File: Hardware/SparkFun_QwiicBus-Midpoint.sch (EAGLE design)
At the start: 39 parts, among them J1 QWIIC, J2 QWIIC, J3 RJ45, J7 RJ45, U1 PCA9615, U2 3.3V

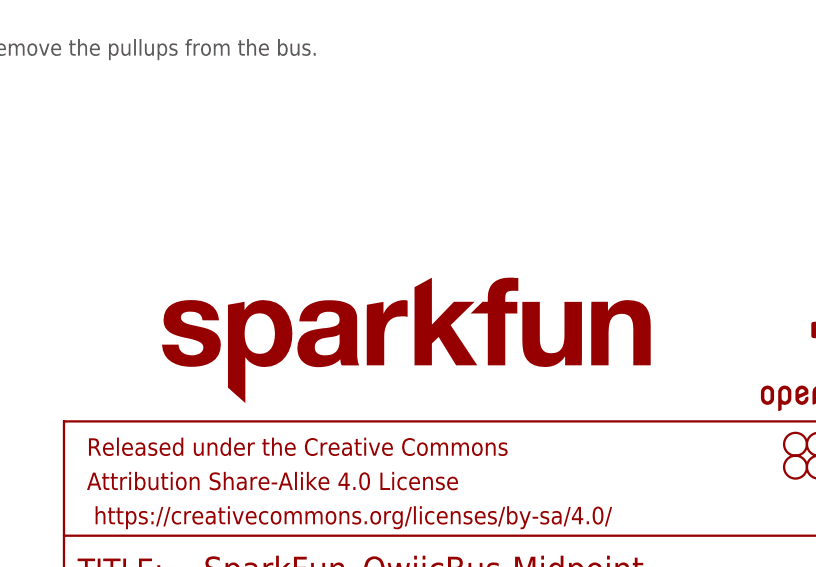
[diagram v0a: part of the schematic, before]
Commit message: adding qwiicBus silk
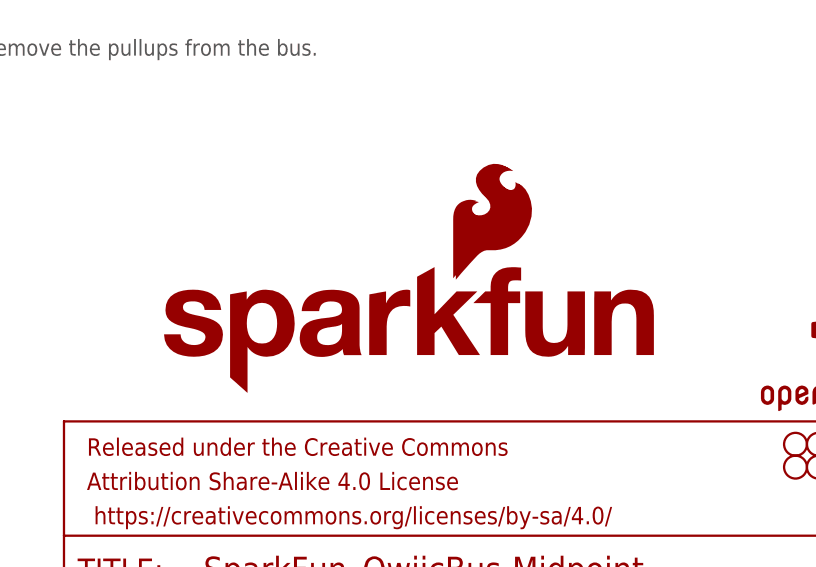
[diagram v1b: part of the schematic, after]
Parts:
- removed LOGO5: SFE_LOGO_NAME.1_INCH, SparkFun-Aesthetics:SFE_LOGO_NAME.1_INCH
- added LOGO3: SFE_LOGO_FLAME.2_INCH, SparkFun-Aesthetics:SFE_LOGO_FLAME.2_INCH
- added LOGO4: SFE_LOGO_NAME_FLAME.1_INCH, SparkFun-Aesthetics:SFE_LOGO_NAME_FLAME.1_INCH
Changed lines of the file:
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@@
 <part name="FD3" library="SparkFun-Aesthetics" deviceset="FIDUCIAL" device="UFIDUCIAL"/>
 <part name="FD4" library="SparkFun-Aesthetics" deviceset="FIDUCIAL" device="UFIDUCIAL"/>
-<part name="LOGO5" library="SparkFun-Aesthetics" deviceset="SFE_LOGO_NAME" device=".1_INCH"/>
 <part name="J7" library="SparkFun-Connectors" deviceset="RJ45-8" device="" value="RJ45"/>
 <part name="GND13" library="SparkFun-PowerSymbols" deviceset="GND" device=""/>
@@
 <part name="J5" library="SparkFun-Connectors" deviceset="CONN_04" device="1X04_NO_SILK"/>
 <part name="J6" library="SparkFun-Connectors" deviceset="CONN_02" device="1X02_NO_SILK"/>
+<part name="LOGO3" library="SparkFun-Aesthetics" deviceset="SFE_LOGO_FLAME" device=".2_INCH" value="SFE_LOGO_FLAME.2_INCH"/>
+<part name="LOGO4" library="SparkFun-Aesthetics" deviceset="SFE_LOGO_NAME_FLAME" device=".1_INCH"/>
 </parts>
 <sheets>
@@
 <instance part="FD3" gate="G$1" x="243.84" y="33.02" smashed="yes"/>
 <instance part="FD4" gate="G$1" x="243.84" y="30.48" smashed="yes"/>
-<instance part="LOGO5" gate="G$1" x="156.21" y="37.592" smashed="yes"/>
 <instance part="J7" gate="JP1" x="210.82" y="144.78" smashed="yes">
 <attribute name="NAME" x="205.74" y="155.448" size="1.778" layer="95" font="vector"/>
@@
 <attribute name="NAME" x="53.34" y="13.208" size="1.778" layer="95" font="vector"/>
 </instance>
+<instance part="LOGO3" gate="G$1" x="190.5" y="50.8" smashed="yes"/>
+<instance part="LOGO4" gate="G$1" x="157.734" y="38.354" smashed="yes"/>
 </instances>
 <busses>

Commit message: pushing mid checklist changes
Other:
- note added: "v11"
- note removed: "v10"
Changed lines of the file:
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@@
 <wire x1="88.9" y1="114.3" x2="0" y2="114.3" width="0.2032" layer="97" style="longdash"/>
 <wire x1="88.9" y1="185.42" x2="88.9" y2="114.3" width="0.2032" layer="97" style="longdash"/>
-<text x="238.76" y="7.62" size="2.54" layer="94" font="vector">v10</text>
+<text x="238.76" y="7.62" size="2.54" layer="94" font="vector">v11</text>
 <wire x1="88.9" y1="81.28" x2="0" y2="81.28" width="0.2032" layer="97" style="longdash"/>
 <text x="114.3" y="76.2" size="1.778" layer="97" font="vector">Cut the I2C jumper to remove the pullups from the bus.</text>

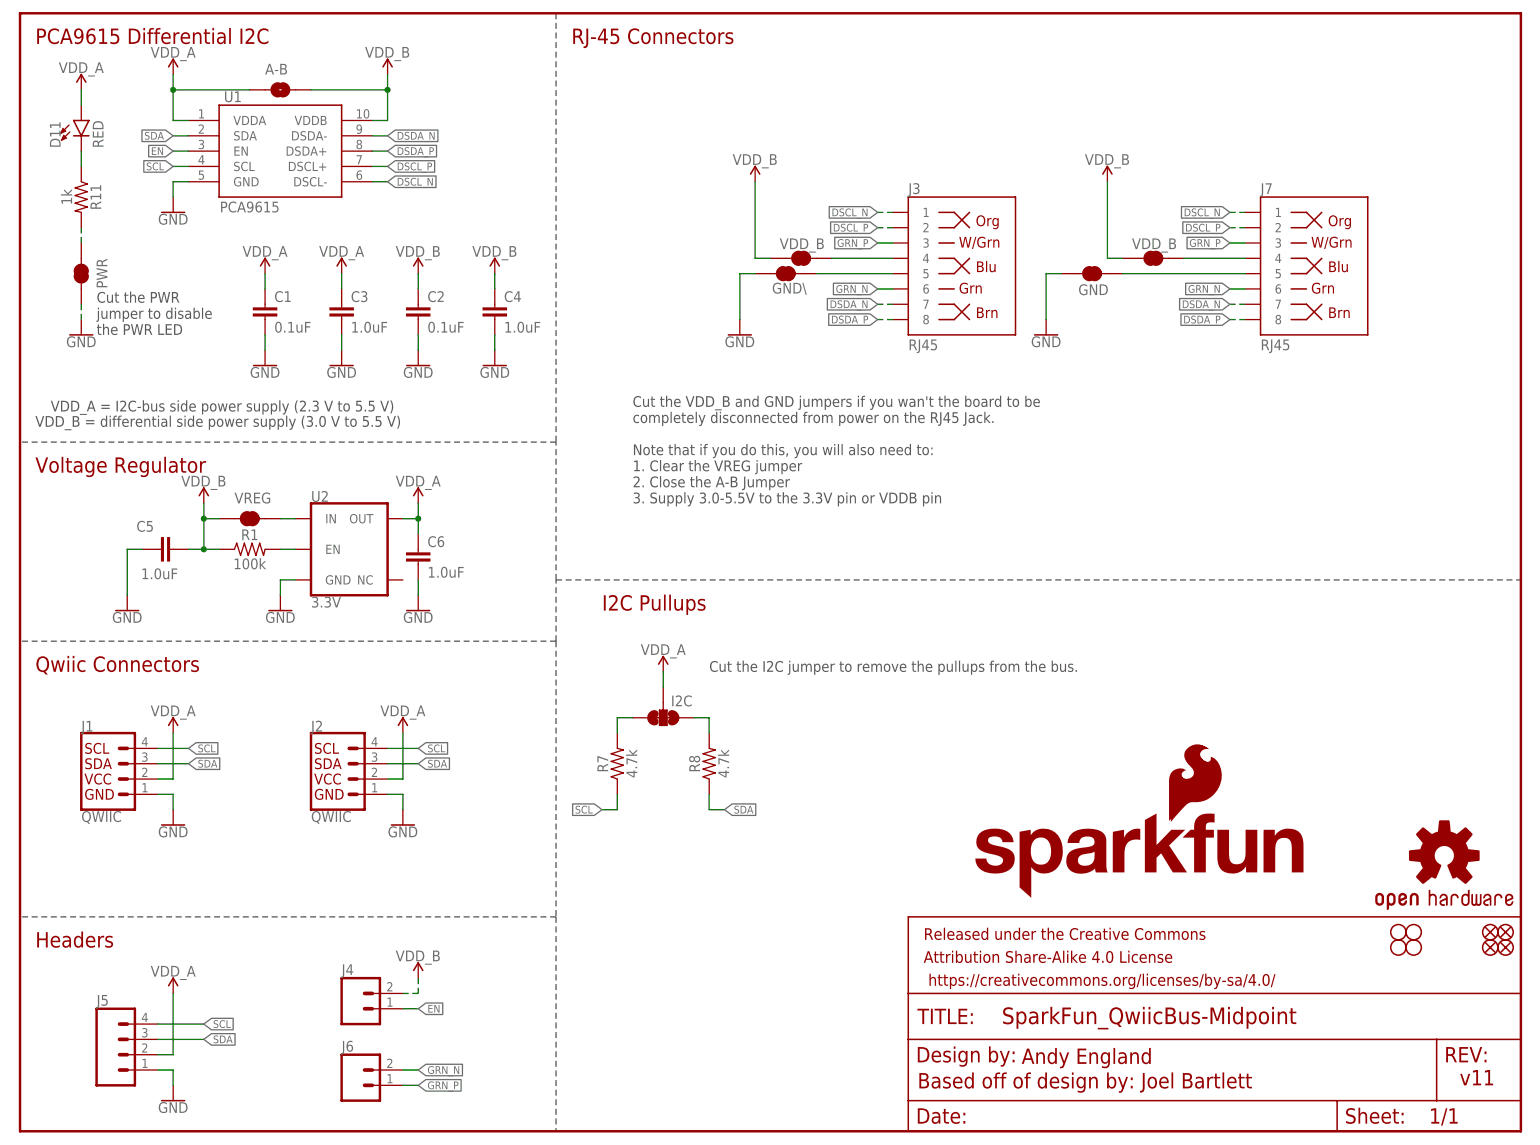
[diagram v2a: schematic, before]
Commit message: adding buck regulator
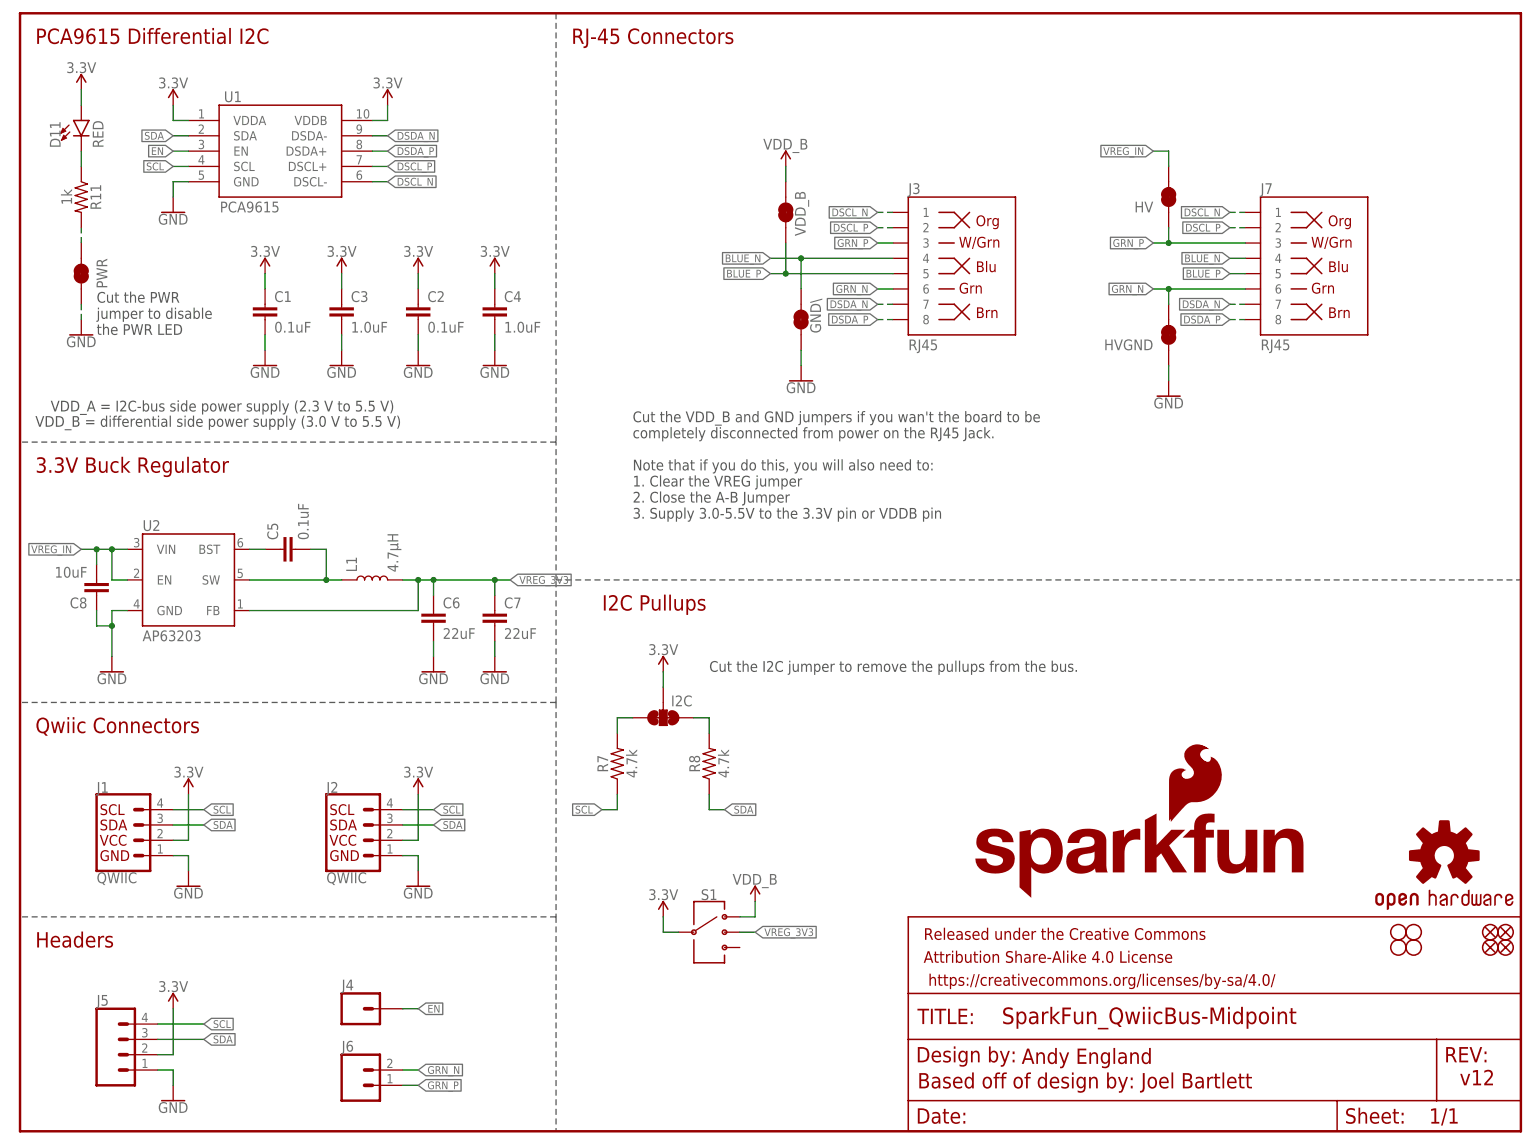
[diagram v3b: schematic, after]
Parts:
- removed A-B: JUMPER-SMT_2_NO_SILK, SparkFun-Jumpers:JUMPER-SMT_2_NO_SILK
- removed JP5, JP6, VREG: JUMPER-SMT_2_NC_TRACE_SILK, SparkFun-Jumpers:JUMPER-SMT_2_NC_TRACE_SILK
- removed R1: 100k, SparkFun-Resistors:100KOHM-0603-1/10W-1%
- added C7: 22uF, SparkFun-Capacitors:22UF-1206-50V-10%
- added C8: 10uF, SparkFun-Capacitors:10UF-1210-50V-20%
- added HV, HVGND: JUMPER-SMT_2_NC_TRACE_SILK, SparkFun-Jumpers:JUMPER-SMT_2_NC_TRACE_SILK
- added L1: 4.7μH, SparkFun-Coils:4.7μH_SHIELDED_INDUCTORNPIS_LS
- added S1: (no value), SparkFun-Switches:SWITCH-SP3T-SMD
- C5: value 1.0uF -> 0.1uF; device SparkFun-Capacitors:1.0UF-0603-16V-10% -> SparkFun-Capacitors:0.1UF-0603-100V-10%
- C6: value 1.0uF -> 22uF; device SparkFun-Capacitors:1.0UF-0603-16V-10% -> SparkFun-Capacitors:22UF-1206-50V-10%
- J4: device SparkFun-Connectors:CONN_021X02_NO_SILK -> SparkFun-Connectors:CONN_01PTH_NO_SILK_YES_STOP
- U2: value 3.3V -> AP63203; device SparkFun-IC-Power:V_REG_AP2112K-3.3V -> SparkFun-IC-Power:AP63203
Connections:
- removed net N$1: J3.4, VDD_B.2
- removed net N$2: GND\.2, J3.5
- removed net N$5: J7.4, JP5.2
- removed net N$6: J7.5, JP6.2
- removed net VDD_A: A-B.1, C1.1, C3.1, C6.1, D11.A, I2C.2, J1.2, J2.2, J5.2, U1.VDDA, U2.OUT
- new net 3.3V: C1.1, C2.1, C3.1, C4.1, D11.A, I2C.2, J1.2, J2.2, J5.2, S1.3, U1.VDDA, U1.VDDB
- new net BLUE_N: GND\.2, J3.4, J7.4
- new net BLUE_P: J3.5, J7.5, VDD_B.2
- new net VREG_3V3: C6.1, C7.1, L1.2, S1.2, U2.FB
- new net VREG_IN: C8.2, HV.2, U2.EN, U2.VIN
- net GND: now also C7.2, C8.1, HVGND.1; no longer C5.1, JP6.1
- net GRN_N: now also HVGND.2
- net GRN_P: now also HV.1
- net N$7: now also C5.1, U2.BST; no longer R1.2, U2.EN
- net N$8: now also C5.2, L1.1, U2.SW; no longer U2.IN, VREG.2
- net VDD_B: now also S1.1; no longer A-B.2, C2.1, C4.1, C5.2, J4.2, JP5.1, R1.1, U1.VDDB, VREG.1
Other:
- note added: "3.3V Buck Regulator"
- note added: "v12"
- note removed: "GND"
- note removed: "VDD_B"
- note removed: "Voltage Regulator"
- note removed: "v11"
- moved on the sheet: C5, C6, GND\, J1, J2, VDD_B

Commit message: post review changes
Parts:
- removed H1: STAND-OFF, SparkFun-Hardware:STAND-OFF
- removed HV, HVGND, VDD_B: JUMPER-SMT_2_NC_TRACE_SILK, SparkFun-Jumpers:JUMPER-SMT_2_NC_TRACE_SILK
- added HV_GND, HV_IN, VDD_A: JUMPER-SMT_2_NC_TRACE_SILK, SparkFun-Jumpers:JUMPER-SMT_2_NC_TRACE_SILK
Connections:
- removed net VDD_B: S1.1, VDD_B.1
- new net VDD_A: S1.1, VDD_A.1
- net BLUE_P: now also VDD_A.2; no longer VDD_B.2
- net GND: now also HV_GND.1; no longer HVGND.1
- net GRN_N: now also HV_GND.2; no longer HVGND.2
- net GRN_P: now also HV_IN.1; no longer HV.1
- net VREG_IN: now also HV_IN.2; no longer HV.2
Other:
- note added: "3.3V 2A Buck Regulator"
- note added: "Be sure to only close one ground jumper at a time to keep a proper current return path."
- note added: "Blue Pair: Cut jumpers to disconnect VDDA (3.3V) from the EndPoint"
- note added: "Green Pair: Close these jumpers and open the blue pair to use the green pair as the input for the buck converter"
- note added: "Power Input Switch"
- note added: "VIN: 3.8V-32V"
- note removed: "3.3V Buck Regulator"
- note removed: "Cut the VDD_B and GND jumpers if you wan't the board to be completely disconnected from power on the RJ45 Jack. Note that if you do this, you will also need to: 1. Clear the VREG jumper 2. Close the A-B Jumper 3. Supply 3.0-5.5V to the 3.3V pin or VDDB pin"
- note removed: "VDD_A = I2C-bus side power supply (2.3 V to 5.5 V)"
- note removed: "VDD_B = differential side power supply (3.0 V to 5.5 V)"
- moved on the sheet: GND\, I2C, J7, R7, R8, S1

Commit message: ordering protos
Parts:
- HV_GND, HV_IN: value JUMPER-SMT_2_NC_TRACE_SILK -> JUMPER-SMT_2_NO_SILK; device SparkFun-Jumpers:JUMPER-SMT_2_NC_TRACE_SILK -> SparkFun-Jumpers:JUMPER-SMT_2_NO_SILK
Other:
- note added: "Use this switch to switch the 3.3V source between high voltage coming over the green pair, low voltage on the blue pair and none, in which case the customer would have to provide 3.3V themselves."
- note added: "VIN: 3.0-5.5V"
- moved on the sheet: C1, C2, C3, C4, D11, PWR, R11, S1, U1

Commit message: post FarmHand Review
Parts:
- removed HV_IN: JUMPER-SMT_2_NO_SILK, SparkFun-Jumpers:JUMPER-SMT_2_NO_SILK
- removed L1: 4.7μH, SparkFun-Coils:4.7μH_SHIELDED_INDUCTORNPIS_LS
- removed S1: (no value), SparkFun-Switches:SWITCH-SP3T-SMD
- removed U2: AP63203, SparkFun-IC-Power:AP63203
- removed VDD_A: JUMPER-SMT_2_NC_TRACE_SILK, SparkFun-Jumpers:JUMPER-SMT_2_NC_TRACE_SILK
- added BUCK_BP: JUMPER-SMT_2_NC_TRACE_SILK, SparkFun-Jumpers:JUMPER-SMT_2_NC_TRACE_SILK
- added C10, C11: 22UF, SparkFun-Capacitors:22UF-1210-16V-20%
- added C12: 100uF, SparkFun-Capacitors:100UF-POLAR-8X10.5-50V
- added C14, C9: 0.1uF, SparkFun-Capacitors:0.1UF-0603-100V-10%
- added C15: 0.22uF, SparkFun-Capacitors:0.22UF-0603-25V-10%
- added L2: 4.7μH, SparkFun-Coils:4.7μH_SHIELDED_INDUCTORNPIS_LS
- added PSEL: JUMPER-SMT_3_NO_SILK, SparkFun-Jumpers:JUMPER-SMT_3_NO_SILK
- added R1, R3: 100k, SparkFun-Resistors:100KOHM-0603-1/10W-1%
- added R2: 43k, SparkFun-Resistors:43KOHM-0603-1/10W-1%
- added TP1: TEST-POINT3, SparkFun-Connectors:TEST-POINT3
- added U3: LMR33630, SparkFun-IC-Power:LMR33630
- C5: value 0.1uF -> 1.0uF; device SparkFun-Capacitors:0.1UF-0603-100V-10% -> SparkFun-Capacitors:1.0UF-0603-16V-10%
- C6, C7: value 22uF -> 4.7uF; device SparkFun-Capacitors:22UF-1206-50V-10% -> SparkFun-Capacitors:4.7UF-0805-50V-(10%)
- C8: value 10uF -> 0.22uF; device SparkFun-Capacitors:10UF-1210-50V-20% -> SparkFun-Capacitors:0.22UF-0603-25V-10%
- HV_GND: value JUMPER-SMT_2_NO_SILK -> JUMPER-SMT_2_NC_TRACE_SILK; device SparkFun-Jumpers:JUMPER-SMT_2_NO_SILK -> SparkFun-Jumpers:JUMPER-SMT_2_NC_TRACE_SILK
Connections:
- removed net BLUE_P: J3.5, J7.5, VDD_A.2
- removed net GRN_P: HV_IN.1, J3.3, J6.1, J7.3
- removed net N$8: C5.2, L1.1, U2.SW
- removed net VDD_A: S1.1, VDD_A.1
- removed net VREG_3V3: C6.1, C7.1, L1.2, S1.2, U2.FB
- new net N$1: C9.1, U3.BOOT
- new net N$6: R1.1, R2.2, U3.FB
- new net N$9: C5.1, R3.2, U3.VCC
- new net SW: C9.2, L2.1, U3.NC, U3.SW
- new net VCC_1: BUCK_BP.2, J3.4, J7.4, PSEL.3, TP1.1, U1.VDDB
- new net VCC_2: J3.3, J6.1, J7.3, PSEL.1
- net 3.3V: now also BUCK_BP.1, C10.1, C11.1, C14.1, L2.2, R1.2; no longer S1.3, U1.VDDB
- net BLUE_N: now also J3.5, J7.5; no longer J3.4, J7.4
- net GND: now also C10.2, C11.2, C12.-, C14.2, C15.2, C5.2, C8.2, R2.1, U3.AGND, U3.PGND; no longer C8.1, U2.GND
- net N$7: now also R3.1, U3.PGOOD; no longer C5.1, U2.BST
- net VREG_IN: now also C12.+, C15.1, C6.1, C7.1, C8.1, PSEL.2, U3.EN, U3.VIN; no longer C8.2, HV_IN.2, U2.EN, U2.VIN
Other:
- note added: "3.8-36V In, 3.3V 3A Out Buck Regulator"
- note added: "Close the VCC2 side of the jumper to power the buck regulator with a high voltage from your HV+/- pins. Close the VCC1 side of the jumper to power the buck regulator with 5V coming from VCC1 on the Endpoint"
- note added: "Jumpers"
- note removed: "3.3V 2A Buck Regulator"
- note removed: "Be sure to only close one ground jumper at a time to keep a proper current return path."
- note removed: "Blue Pair: Cut jumpers to disconnect VDDA (3.3V) from the EndPoint"
- note removed: "Green Pair: Close these jumpers and open the blue pair to use the green pair as the input for the buck converter"
- note removed: "I2C Pullups"
- note removed: "Power Input Switch"
- note removed: "Use this switch to switch the 3.3V source between high voltage coming over the green pair, low voltage on the blue pair and none, in which case the customer would have to provide 3.3V themselves."
- moved on the sheet: C5, C6, C7, C8, GND\, I2C, J1, J2, J3, J7, R7, R8

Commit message: post checklist changes
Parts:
- removed BUCK_BP: JUMPER-SMT_2_NC_TRACE_SILK, SparkFun-Jumpers:JUMPER-SMT_2_NC_TRACE_SILK
- added BP: JUMPER-SMT_2_NC_TRACE_SILK, SparkFun-Jumpers:JUMPER-SMT_2_NC_TRACE_SILK
- C10, C11: value 22UF -> 22uF
- C15, C8: device SparkFun-Capacitors:0.22UF-0603-25V-10% -> SparkFun-Capacitors:0.22UF-0603-50V-10%
- L2: value 4.7μH -> 2.2uH; device SparkFun-Coils:4.7μH_SHIELDED_INDUCTORNPIS_LS -> SparkFun-Coils:2.2μH_SHIELDED_INDUCTOR_5X5
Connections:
- net 3.3V: now also BP.1; no longer BUCK_BP.1
- net VCC_1: now also BP.2; no longer BUCK_BP.2
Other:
- note added: "Depending on load and distance requirements, there are several different ways to power the Midpoint/Endpoint combo. --- The default option powers the entire system using 3.3V, in this configuration, the BP jumper is closed and both sides of the PSEL jumper are open. --- To power the VCC_1 rail with 5V (The PCA9615 operates better at this voltage), the BP jumper must be opened. Then close the "1" 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"
- note added: "GRN wire is connected to Ground for high voltage VCC2 while W/GRN wire is connected to VCC2"
- note added: "If anything other than 3.3V is used, BP MUST be cut/open"
- note added: "v13"
- note removed: "Close the VCC2 side of the jumper to power the buck regulator with a high voltage from your HV+/- pins. Close the VCC1 side of the jumper to power the buck regulator with 5V coming from VCC1 on the Endpoint"
- note removed: "v12"
- moved on the sheet: C10, C11, C12, C14, C15, C5, C6, C7, C8, C9, GND\, HV_GND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

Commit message: initial layout of hot swap controller
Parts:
- added C13: 20nF, hotswap:20NF-0603-50V-10%
- added C17: 39nF, hotswap:39NF-0805-50V-10%
- added D1: SMAJ36A, hotswap:DIODE_TVS_UNI
- added FRAME2: FRAME-LETTER, SparkFun-Aesthetics:FRAME-LETTER
- added Q1: SI7120AD, hotswap:SI7120AD
- added R10: 23m, hotswap:23MILLIOHM
- added R12: 10, SparkFun-Resistors:10OHM-0603-1/10W-1%
- added R13: 1k, SparkFun-Resistors:1KOHM-0603-1/10W-1%
- added R14: 20k, SparkFun-Resistors:20KOHM-0603-1/10W-1%
- added R15: 1M, SparkFun-Resistors:1MOHM-0603-1/4W-5%
- added R4: 1.65K, hotswap:1.65KOHM
- added R5: 32.4k, hotswap:32.4KOHM
- added R6: 4.22k, hotswap:4.22KOHM
- added R9: 1020K, hotswap:1020KOHM
- added U4: LTC4231 Hot Swap Controller, hotswap:LTC4231
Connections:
- new net N$10: R4.2, R9.1, U4.UVL
- new net N$11: Q1.G, R12.2
- new net N$12: Q1.D, R10.2, U4.SENSE
- new net N$16: R12.1, R13.2, U4.GATE
- new net N$17: C13.1, R13.1
- new net N$19: R14.1, U4.STATUS
- new net N$2: R5.1, U4.GNDSW
- new net N$20: R15.1, U4.!SHDN
- new net N$21: C17.1, U4.TIMER
- new net N$5: R5.2, R6.1, U4.OV
- new net N$8: R4.1, R6.2, U4.UVH
- new net PWR_SRC: D1.C, PSEL.2, R10.1, R15.2, R9.2, U4.IN
- net GND: now also C13.2, C17.2, D1.A, U4.GND
- net VREG_IN: now also Q1.S, R14.2, U4.SOURCE; no longer PSEL.2
